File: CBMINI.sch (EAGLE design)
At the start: 57 parts, among them IC1 ATMEGA32U4NT, IC2 MCP2515, IC3 MCP2551, J1 USB_B_PTH, SW1 SWITCH-DPDT3, X1 INPUT, X2 OUTPUT

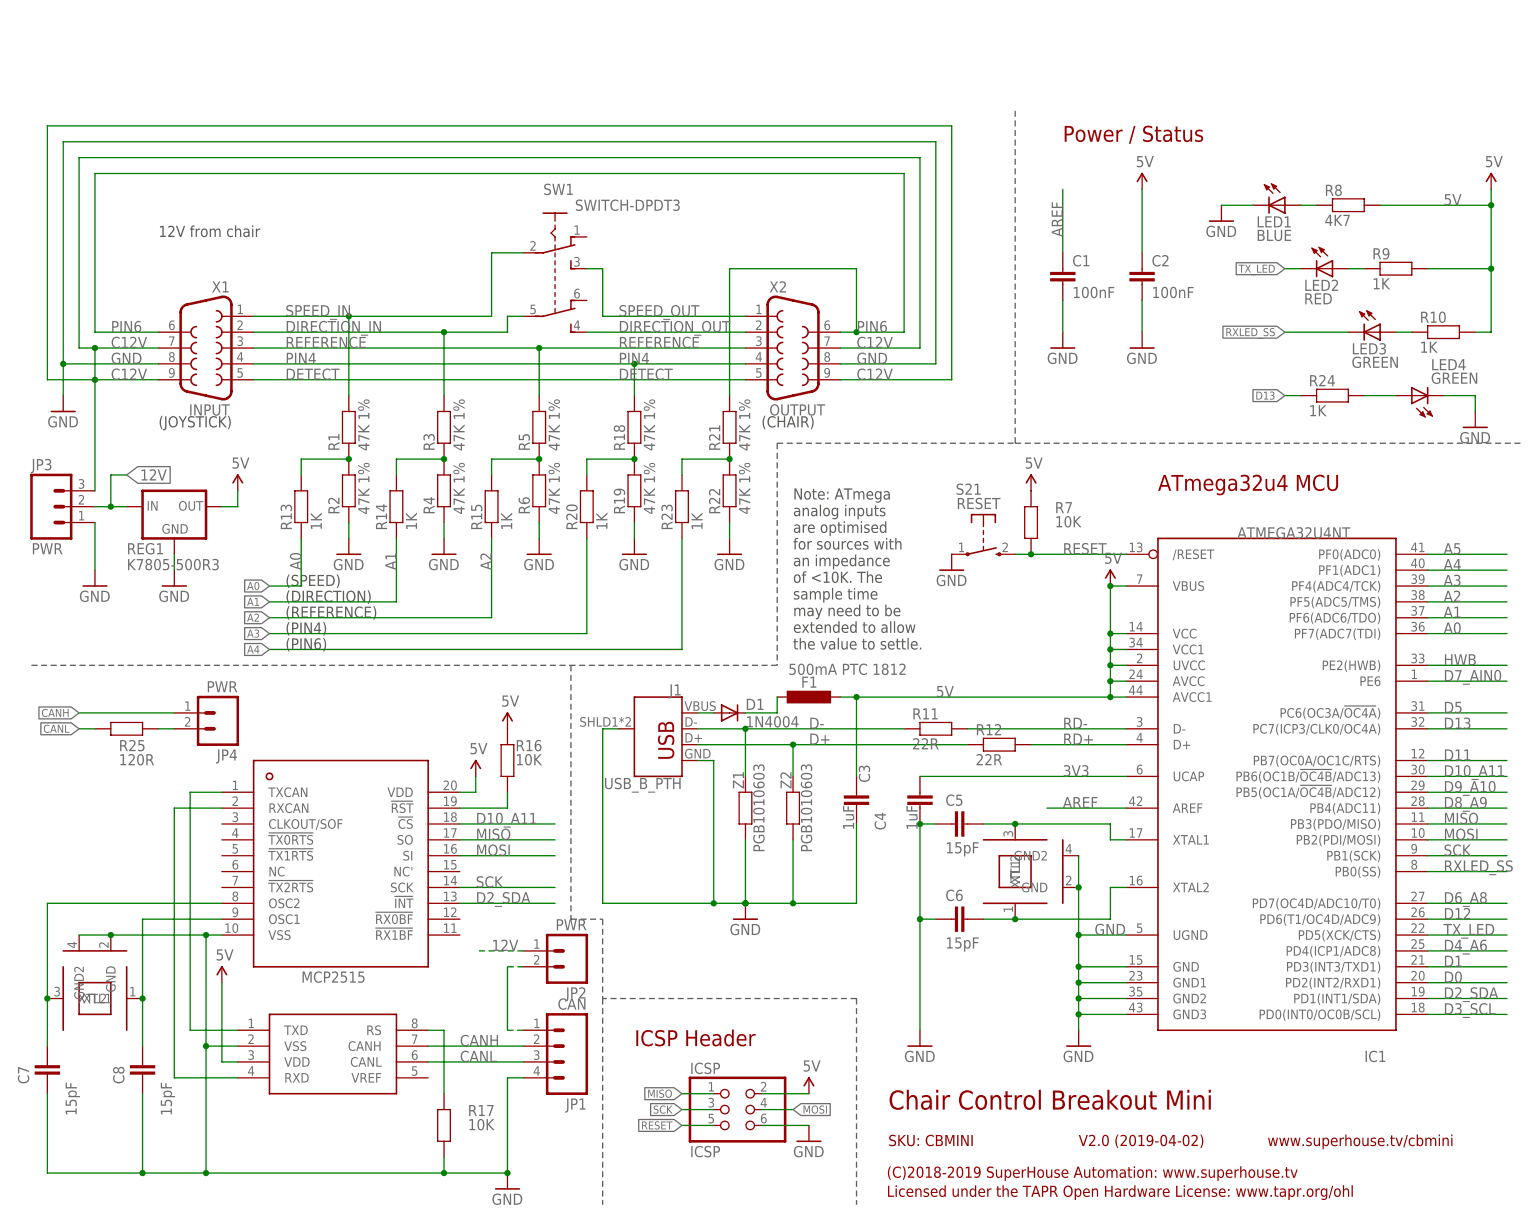
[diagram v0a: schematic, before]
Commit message: Changed input 5 to pin 5 for v2.1 release
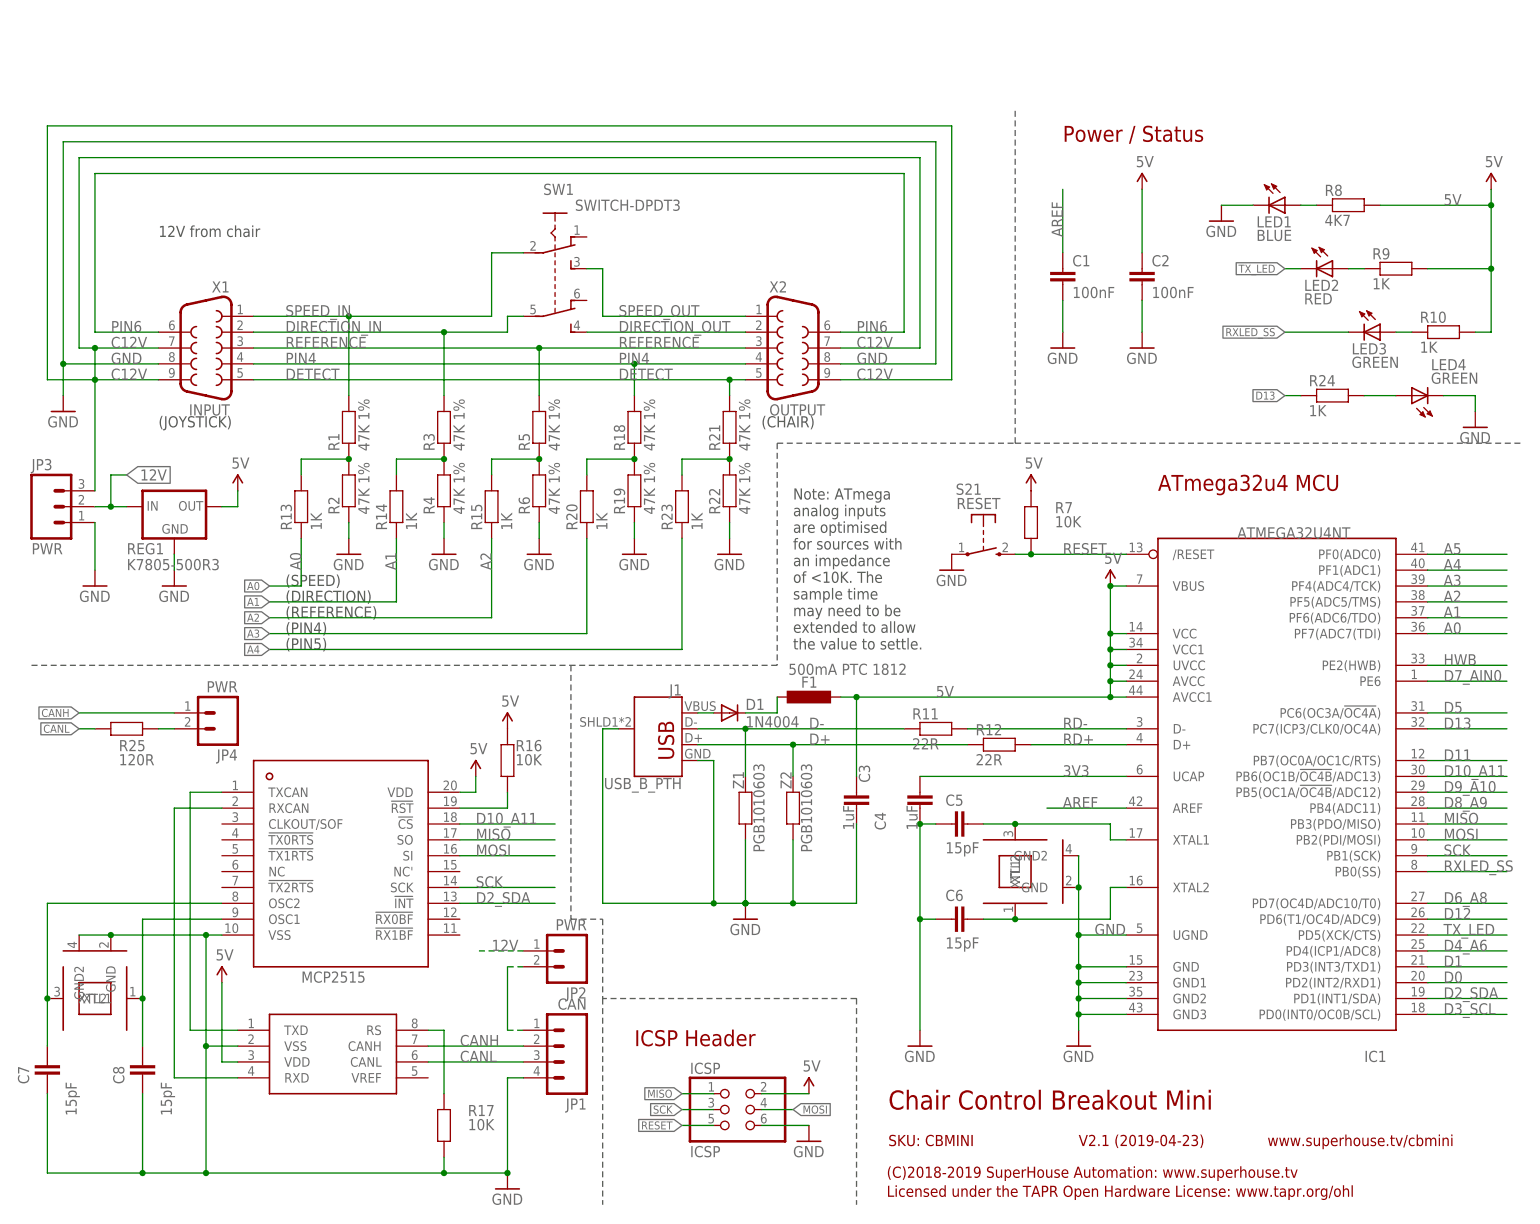
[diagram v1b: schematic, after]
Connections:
- net DETECT: now also R21.2
- net PIN6: no longer R21.2
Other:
- note added: "(PIN5)"
- note added: "V2.1 (2019-04-23)"
- note removed: "(PIN6)"
- note removed: "V2.0 (2019-04-02)"
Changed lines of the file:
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@@
 <text x="185.42" y="119.38" size="2.54" layer="94" ratio="12">ATmega32u4 MCU</text>
 <text x="142.24" y="20.32" size="3.048" layer="94">Chair Control Breakout Mini</text>
-<text x="172.72" y="14.478" size="1.778" layer="94">V2.0 (2019-04-02)</text>
+<text x="172.72" y="14.478" size="1.778" layer="94">V2.1 (2019-04-23)</text>
 <text x="142.24" y="14.478" size="1.778" layer="94">SKU: CBMINI</text>
 <text x="141.986" y="9.398" size="1.778" layer="94">(C)2018-2019 SuperHouse Automation: www.superhouse.tv</text>
@@
 <wire x1="137.16" y1="38.1" x2="137.16" y2="5.08" width="0.1524" layer="97" style="longdash"/>
 <text x="45.72" y="96.52" size="1.778" layer="97">(PIN4)</text>
-<text x="45.72" y="93.98" size="1.778" layer="97">(PIN6)</text>
+<text x="45.72" y="93.98" size="1.778" layer="97">(PIN5)</text>
 </plain>
 <instances>
@@
 <pinref part="X1" gate="G$1" pin="5"/>
 <pinref part="X2" gate="G$1" pin="5"/>
-<wire x1="40.64" y1="137.16" x2="119.38" y2="137.16" width="0.1524" layer="91"/>
+<wire x1="40.64" y1="137.16" x2="116.84" y2="137.16" width="0.1524" layer="91"/>
 <label x="45.72" y="137.16" size="1.778" layer="95"/>
 <label x="99.06" y="137.16" size="1.778" layer="95"/>
+<pinref part="R21" gate="G$1" pin="2"/>
+<wire x1="116.84" y1="137.16" x2="119.38" y2="137.16" width="0.1524" layer="91"/>
+<wire x1="116.84" y1="134.62" x2="116.84" y2="137.16" width="0.1524" layer="91"/>
+<junction x="116.84" y="137.16"/>
 </segment>
 </net>
@@
 <wire x1="144.78" y1="170.18" x2="144.78" y2="144.78" width="0.1524" layer="91"/>
 <pinref part="X2" gate="G$1" pin="6"/>
-<wire x1="144.78" y1="144.78" x2="137.16" y2="144.78" width="0.1524" layer="91"/>
+<wire x1="144.78" y1="144.78" x2="134.62" y2="144.78" width="0.1524" layer="91"/>
 <label x="17.78" y="144.78" size="1.778" layer="95"/>
 <label x="137.16" y="144.78" size="1.778" layer="95"/>
-<pinref part="R21" gate="G$1" pin="2"/>
-<wire x1="137.16" y1="144.78" x2="134.62" y2="144.78" width="0.1524" layer="91"/>
-<wire x1="116.84" y1="134.62" x2="116.84" y2="154.94" width="0.1524" layer="91"/>
-<wire x1="116.84" y1="154.94" x2="137.16" y2="154.94" width="0.1524" layer="91"/>
-<wire x1="137.16" y1="154.94" x2="137.16" y2="144.78" width="0.1524" layer="91"/>
-<junction x="137.16" y="144.78"/>
-</segment>
-</net>
+</segment>
+</net>

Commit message: Clickety click, replace replace
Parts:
- removed S21: RESET, freetronics-jon:TAC_SWITCH_2PINSMT
- added S1: RESET, SuperHouse-Switches:TAC_SWITCH_2PINSMT
- C1, C2, C3, C4, C5, C6, C7, C8: device freetronics-master-v1.1:CAP0603 -> SuperHouse-DiscreteSemi:CAP0603
- D1: device freetronics-jon:DIODESMB -> SuperHouse-DiscreteSemi:DIODESMA
- F1: device rcl:L-EUL1812 -> SuperHouse-Fuses:PTC050
- IC1: value ATMEGA32U4NT -> ATMEGA32U4NT-TQFP; device freetronics-jon:ATMEGA32U4NT -> SuperHouse-MCUs:ATMEGA32U4NT-TQFP
- IC2: device MCP2515:MCP2515 -> SuperHouse-ICs:MCP2515
- IC3: device freetronics-original:MCP2551 -> SuperHouse-ICs:MCP2551
- ICSP: device pinhead:PINHD-2X3 -> SuperHouse-Connectors:ICSP-PIN
- J1: value USB_B_PTH -> USB-B-PTH; device SparkFun-Connectors:USB_B_PTH -> SuperHouse-Connectors:USB-B-PTH
- JP1: device freetronics-jon:M04PTH -> SuperHouse-Connectors:M04-PIN
- JP2, JP4: device freetronics-jon:M02PTH -> SuperHouse-Connectors:M02-PIN
- JP3: device freetronics-jon:M03PTH -> SuperHouse-Connectors:M03-PIN
- LED1, LED2, LED3, LED4: device freetronics-jon:LED0603 -> SuperHouse-LEDs:LED0603
- R1, R10, R11, R12, R13, R14, R15, R18, R19, R2, R20, R21, R22, R23, R24, R3, R4, R5, R6, R8, R9: device freetronics-jon:RESISTOR0603 -> SuperHouse-DiscreteSemi:RESISTOR0603
- R16, R17, R25, R7: device freetronics-master-v1.1:RESISTOR0603 -> SuperHouse-DiscreteSemi:RESISTOR0603
- REG1: device freetronics-jon:K78XX-500R3 -> SuperHouse-Regulators:K78XX-500R3
- XTL1, XTL2: device freetronics-jon:CRYSTAL-GND3X2 -> SuperHouse-Oscillators:CRYSTAL-GND3X2
- Z1, Z2: device freetronics-master-v1.1:RESISTOR0603 -> SuperHouse-DiscreteSemi:TVS0603
- renumbered SW1 to S2
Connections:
- net GND: now also S1.P; no longer S21.P
- net RESET: now also S1.S; no longer S21.S
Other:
- moved on the sheet: JP3

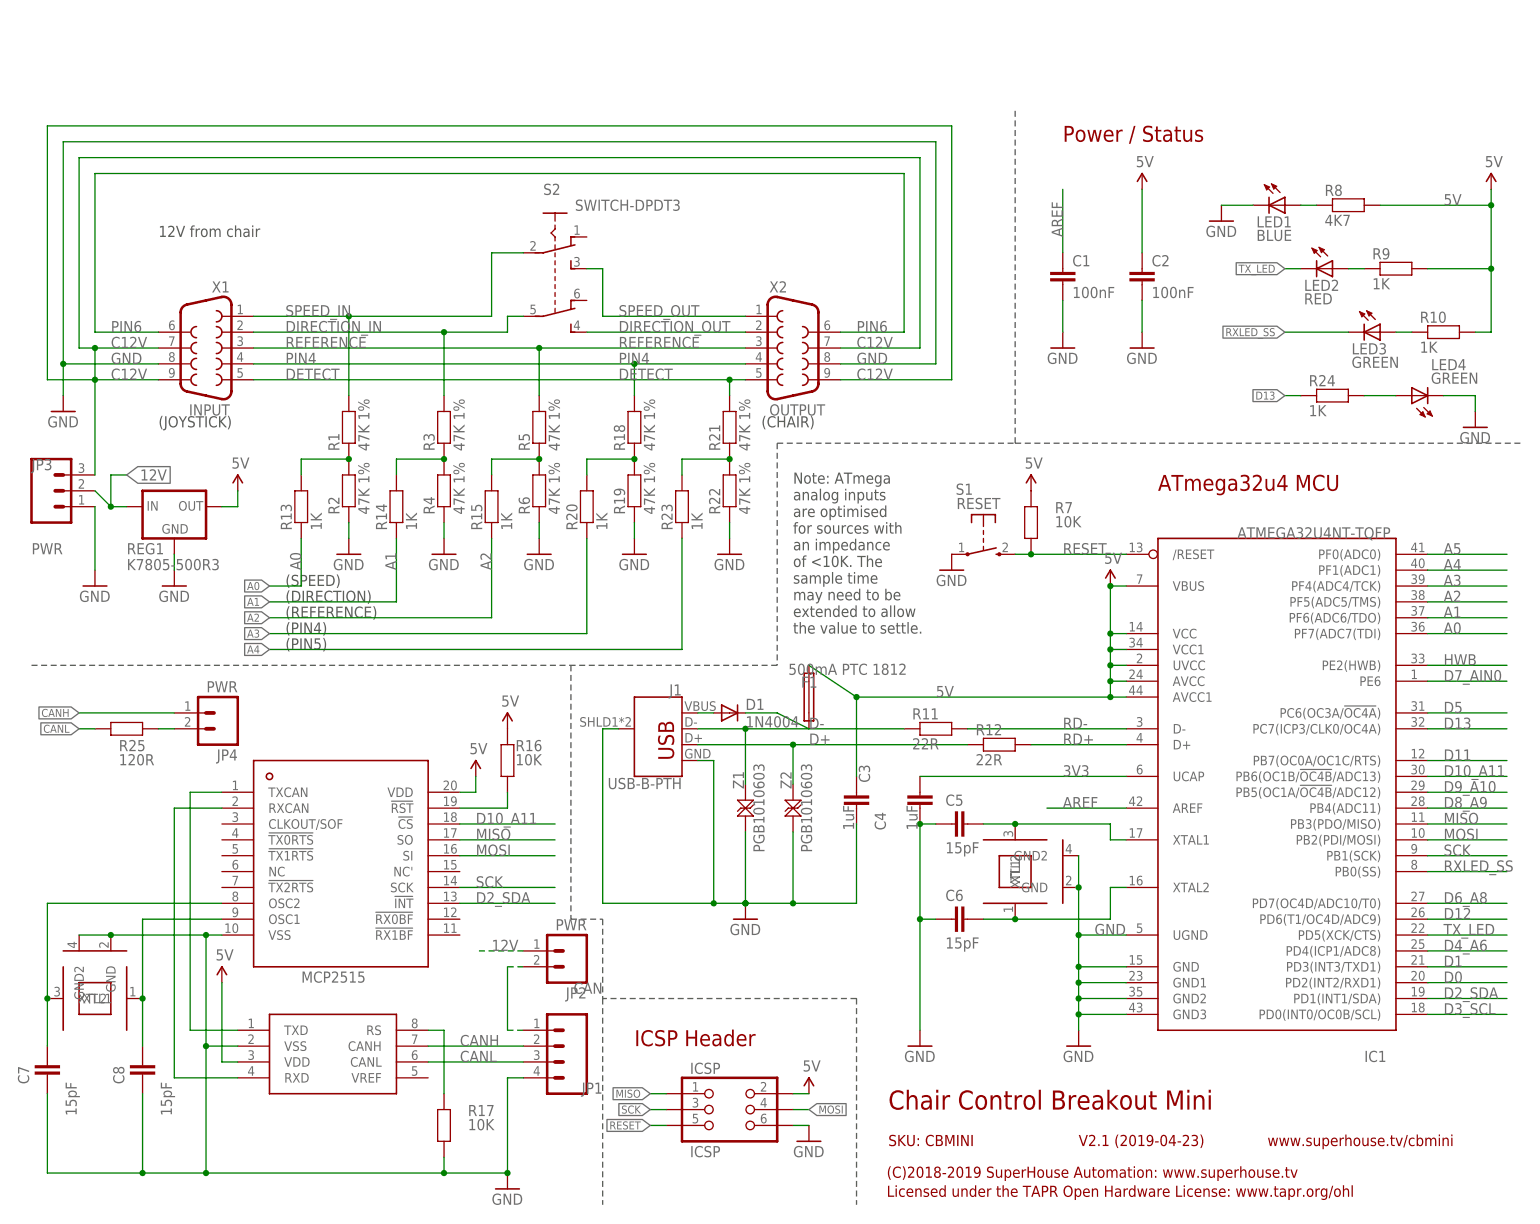
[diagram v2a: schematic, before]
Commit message: Restructured voltage regulators to support 24V CAN or Permobil controller for v2.2 release
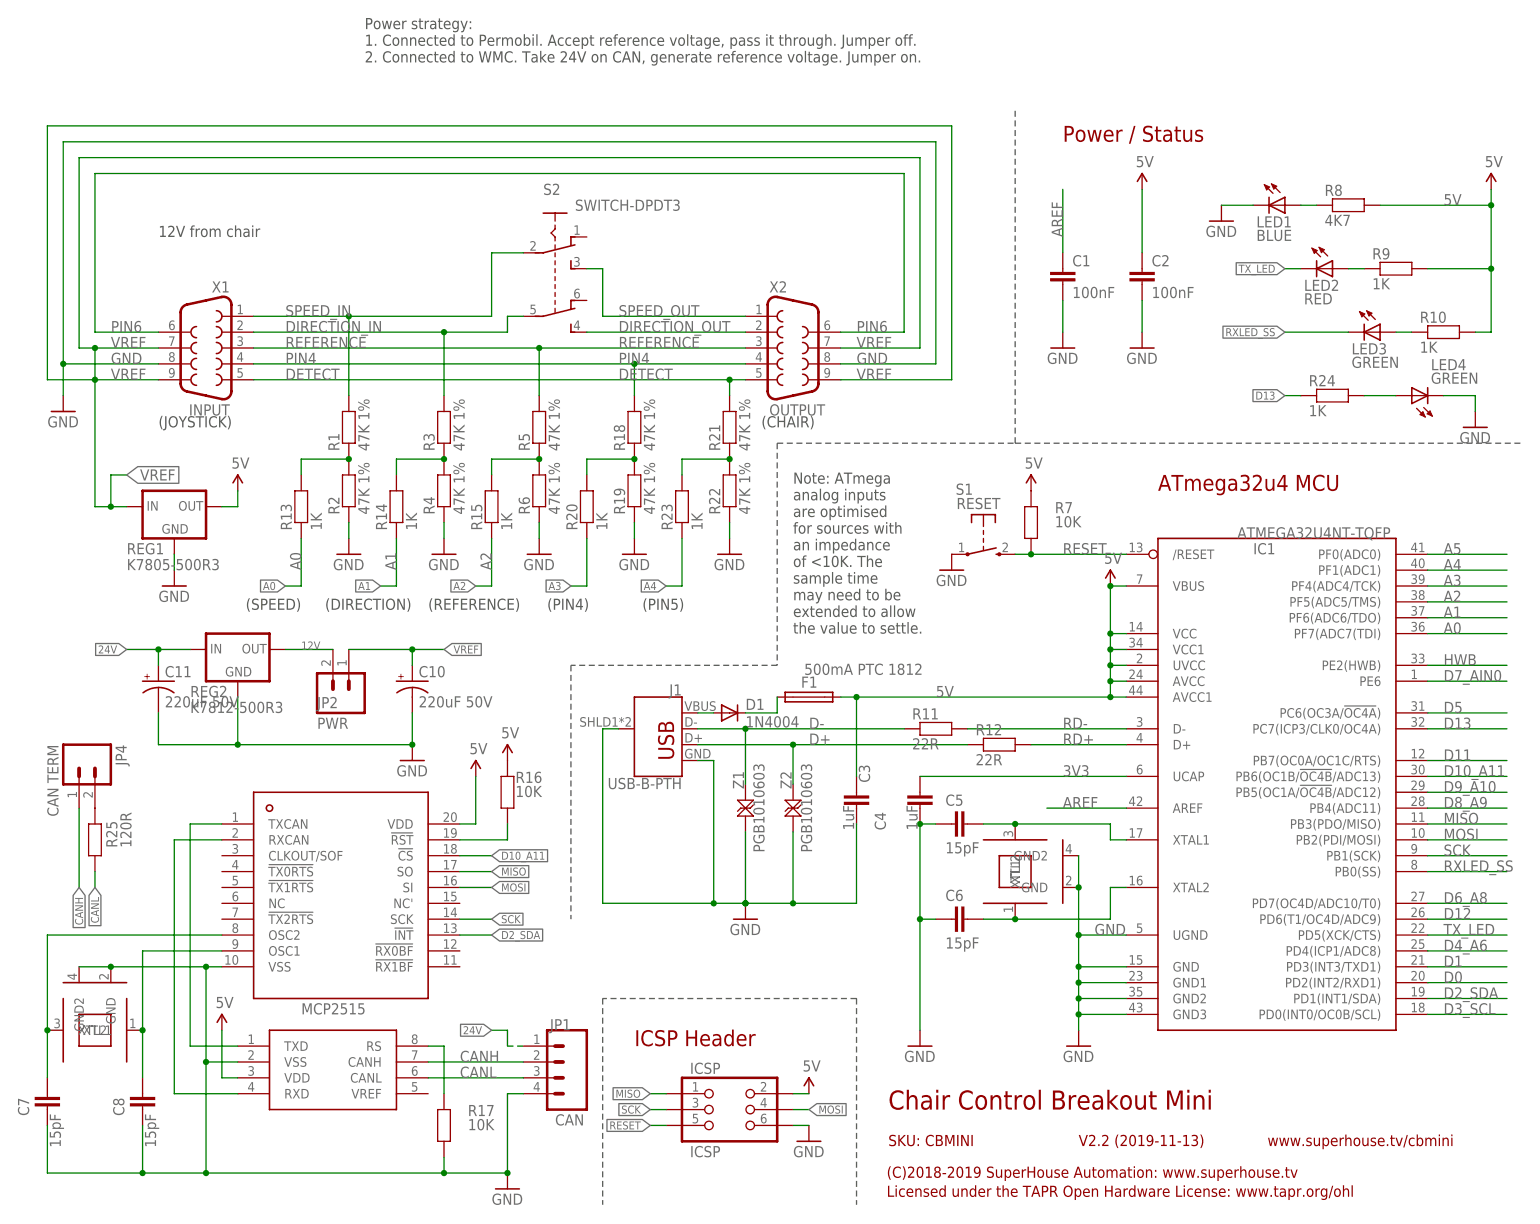
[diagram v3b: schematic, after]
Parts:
- removed JP3: PWR, SuperHouse-Connectors:M03-PIN
- added C10, C11: 220uF 50V, SuperHouse-DiscreteSemi:CAP_POLG
- added REG2: K7812-500R3, SuperHouse-Regulators:K78XX-500R3
- JP4: value PWR -> CAN TERM
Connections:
- removed net C12V: JP3.3, X1.7, X1.9, X2.7, X2.9
- removed net N$15: JP1.1, JP2.2
- new net 24V: C11.+, JP1.1, REG2.IN
- new net VREF: C10.+, JP2.1, REG1.IN, X1.7, X1.9, X2.7, X2.9
- net 12V: now also JP2.2, REG2.OUT; no longer JP2.1, JP3.2, REG1.IN
- net GND: now also C10.-, C11.-, REG2.GND; no longer JP3.1
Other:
- note added: "Power strategy: 1. Connected to Permobil. Accept reference voltage, pass it through. Jumper off. 2. Connected to WMC. Take 24V on CAN, generate reference voltage. Jumper on."
- note added: "V2.2 (2019-11-13)"
- note removed: "V2.1 (2019-04-23)"
- moved on the sheet: C7, C8, F1, JP1, JP2, JP4, R16, R25
